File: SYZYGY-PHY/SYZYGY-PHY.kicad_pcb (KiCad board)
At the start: 4 copper layers, 57.7 x 28 mm, 37 parts, among them J1 QTH-020-01-X-D-DP-A, J2 ARJM11C7-502-KB-EW2, J3 Conn_01x08, U1 GPY111, Y1 Crystal_GND24

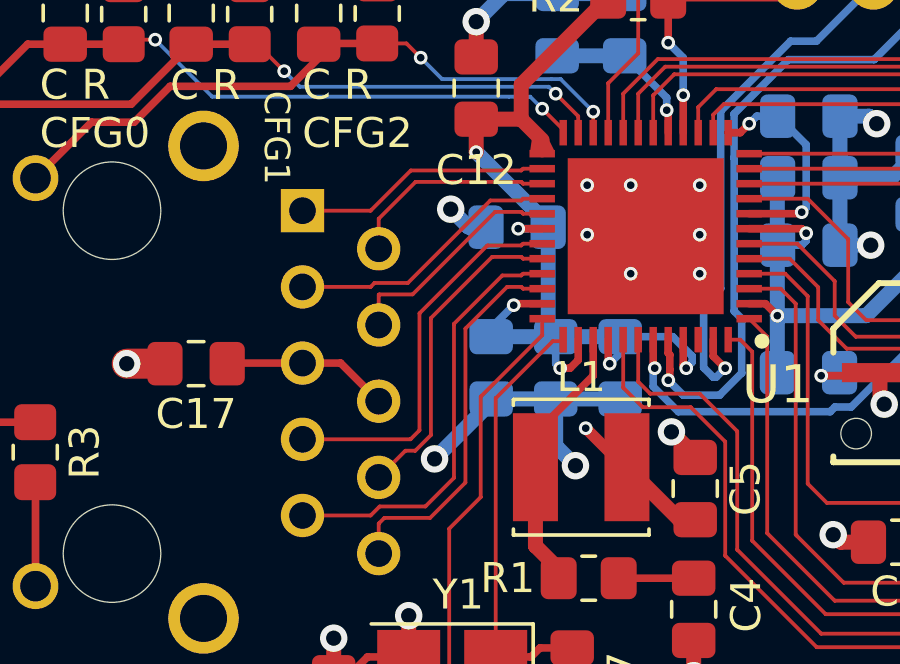
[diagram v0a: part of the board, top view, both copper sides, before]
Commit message: fixing diff pair skew from the twisted pair interface
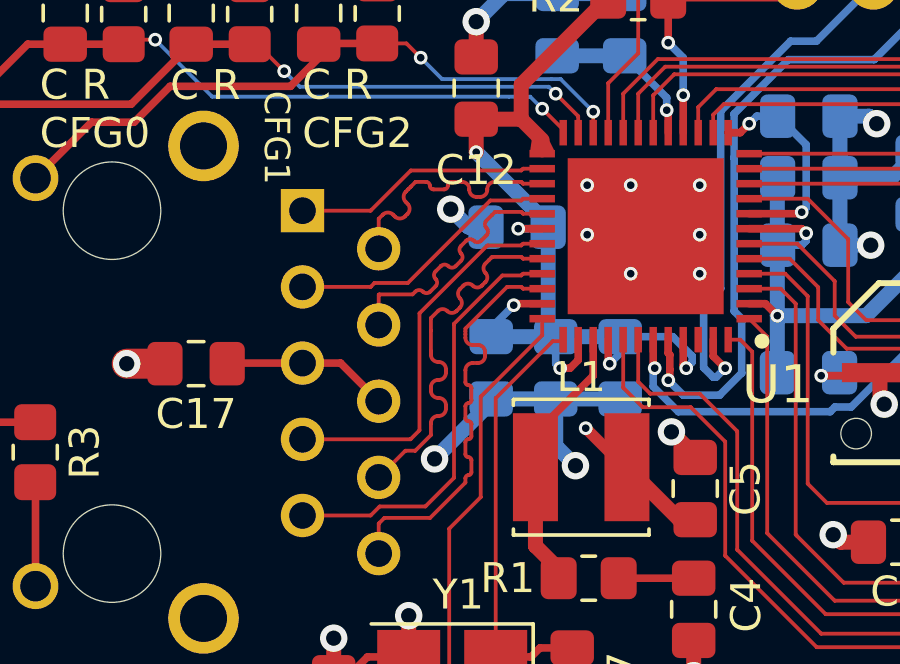
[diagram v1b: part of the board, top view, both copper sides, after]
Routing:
- net /TD3-: track 10.8 -> 12.8 mm
- net /TD4-: track 12.8 -> 14.2 mm
- net /TD1-: track 6.98 -> 8.47 mm
- net /TD2-: track 7.62 -> 8.74 mm

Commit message: syzygy todo update
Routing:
- net GND: vias 35 -> 82

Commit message: wibbly wobbly
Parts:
- removed C3: 10u, Capacitor_SMD:C_0805_2012Metric_Pad1.18x1.45mm_HandSolder
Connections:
- J1 pad 39: +1V8 -> unconnected-(J1-Pad39)
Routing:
- net /TXD3: track 9.62 -> 17.9 mm
- net /TXD2: track 10.4 -> 17.9 mm
- net /RX_CLK: track 18.6 -> 23.8 mm
- net /RXD0: track 19.4 -> 23.8 mm
- net /RXD1: track 19.9 -> 23.9 mm
- net +1V8: track 3.14 -> 0.00 mm, vias 2 -> 0
- net /TXD1: track 14.8 -> 17.8 mm
- net /RXD3: track 25.0 -> 23.9 mm
- net /RXD2: track 24.9 -> 23.8 mm
- net GND: track 80.2 -> 79.8 mm, vias 82 -> 34

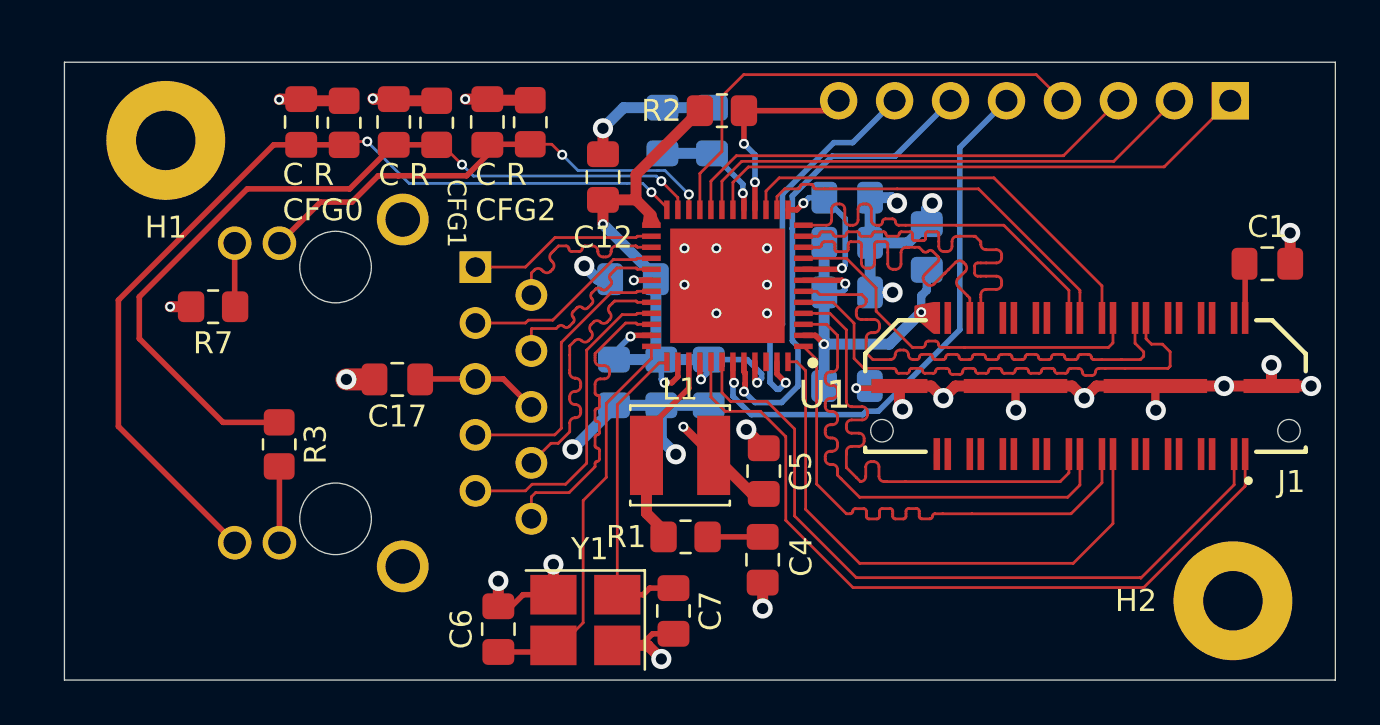
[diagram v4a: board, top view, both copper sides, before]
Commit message: picking a concrete inductor and updating footprint, breakout out MDC/MDIO into headers instead of SYZYGY, corrected rules and text labels
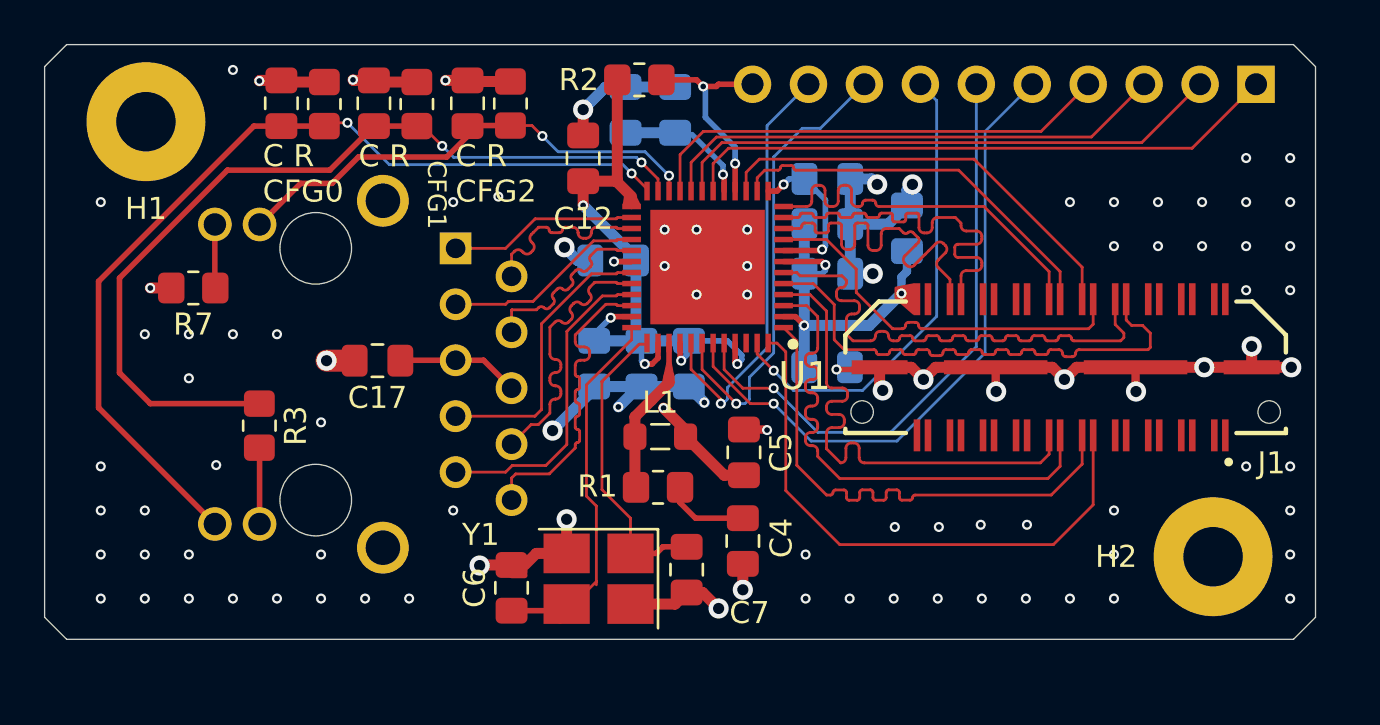
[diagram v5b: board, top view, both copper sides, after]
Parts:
- removed C1: 10u, Capacitor_SMD:C_0805_2012Metric_Pad1.18x1.45mm_HandSolder
- J3: value Conn_01x08 -> Conn_01x10; footprint Connector_PinSocket_2.54mm:PinSocket_1x08_P2.54mm_Vertical -> Connector_PinSocket_2.54mm:PinSocket_1x10_P2.54mm_Vertical
- L1: footprint Inductor_SMD:L_Abracon_ASPI-0425 -> Inductor_SMD:L_0805_2012Metric_Pad1.05x1.20mm_HandSolder
- moved R2 4.00 mm to (117.0, 63.6)
- moved R1 2.57 mm to (117.8, 82.1)
- moved H2 2.19 mm to (143.1, 85.2)
- moved C6 1.97 mm to (111.2, 86.7)
- moved C7 1.97 mm to (119.2, 85.8)
- moved Y1 1.97 mm to (115.2, 86.2)
- moved C16 1.92 mm to (116.4, 65.0)
- moved C18 1.92 mm to (118.6, 65.0)
- moved J3 1.39 mm to (145.0, 63.8)
- moved C13 1.24 mm to (115.8, 71.8)
- moved C15 1.24 mm to (117.1, 76.5)
- moved C17 1.24 mm to (105.1, 76.3)
- moved C19 1.24 mm to (125.5, 68.1)
- moved C20 1.24 mm to (100.8, 64.7)
- moved C8 1.24 mm to (119.2, 76.5)
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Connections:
- J1 pad 01: /MDC -> unconnected-(J1-Pad01)
- J1 pad 02: +5V -> unconnected-(J1-Pad02)
- J1 pad 03: /MDIO -> unconnected-(J1-Pad03)
- J3 pad 8: /RSTN -> /MDIO
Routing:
- net /MDC: track 35.0 -> 19.5 mm, vias 0 -> 1
- net /MDIO: track 33.6 -> 21.0 mm, vias 0 -> 1
- net /SDA: track 22.1 -> 27.4 mm
- net /SCL: track 25.1 -> 29.6 mm
- net /MDINT: track 17.7 -> 21.6 mm
- net GND: track 79.8 -> 77.3 mm, vias 34 -> 96
- net +5V: track 2.47 -> 0.00 mm
- net /REG0: track 9.07 -> 6.61 mm
- net /TCK: track 23.4 -> 25.4 mm
- net /TDI: track 25.4 -> 27.4 mm
- net /TMS: track 21.3 -> 23.3 mm
- net /XTAL1: track 18.2 -> 16.8 mm
- net /LED1: track 38.7 -> 40.1 mm
- net Net-(C4-Pad2): track 2.50 -> 3.84 mm
- net +3V3: track 57.6 -> 57.0 mm
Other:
- board size 57.7 x 28 mm -> 57.7 x 27 mm
- board text added: "MDC"
- board text added: "MDIO"

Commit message: adding another mounting hole for a more stable 3 mounts
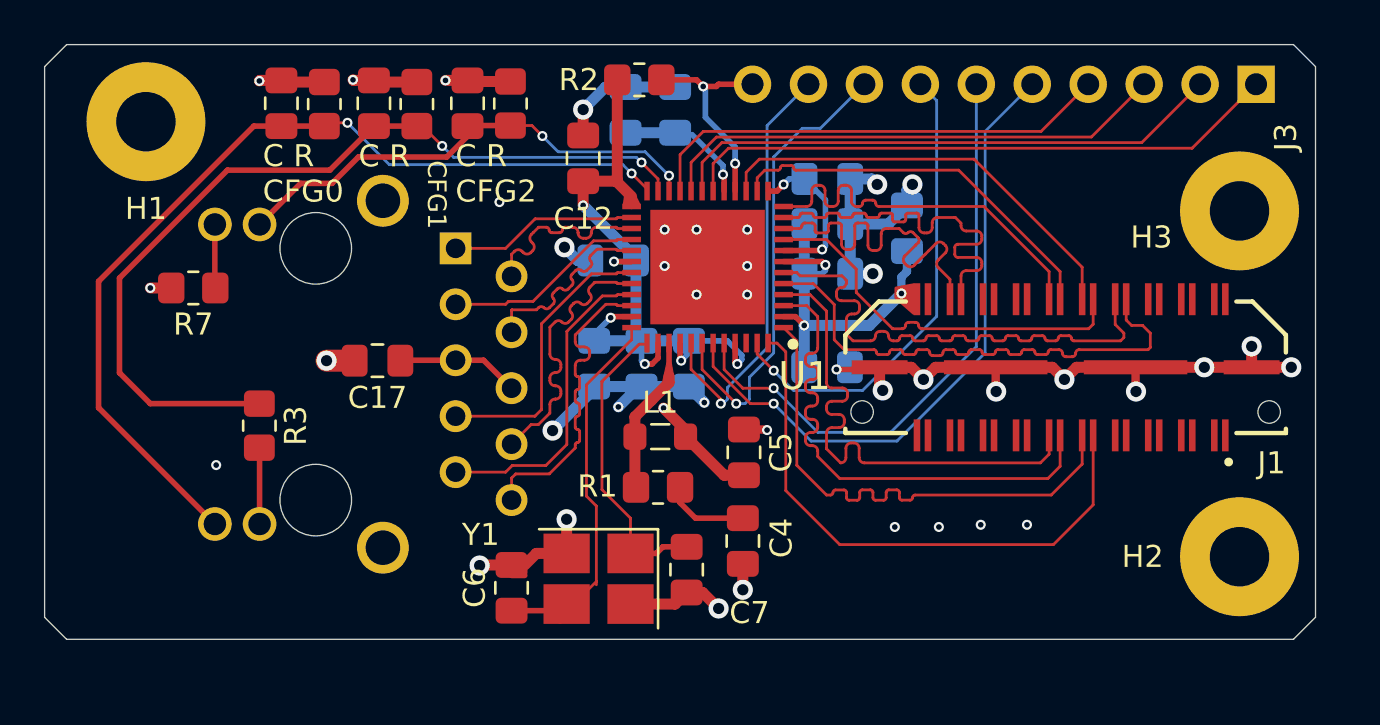
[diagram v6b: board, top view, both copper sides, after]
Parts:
- added H3: MountingHole_Pad, MountingHole:MountingHole_2.7mm_M2.5_Pad, F.Cu at (144.2, 69.5)
- moved H2 1.20 mm to (144.2, 85.2)
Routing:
- net GND: vias 96 -> 40

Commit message: adding GND stippling
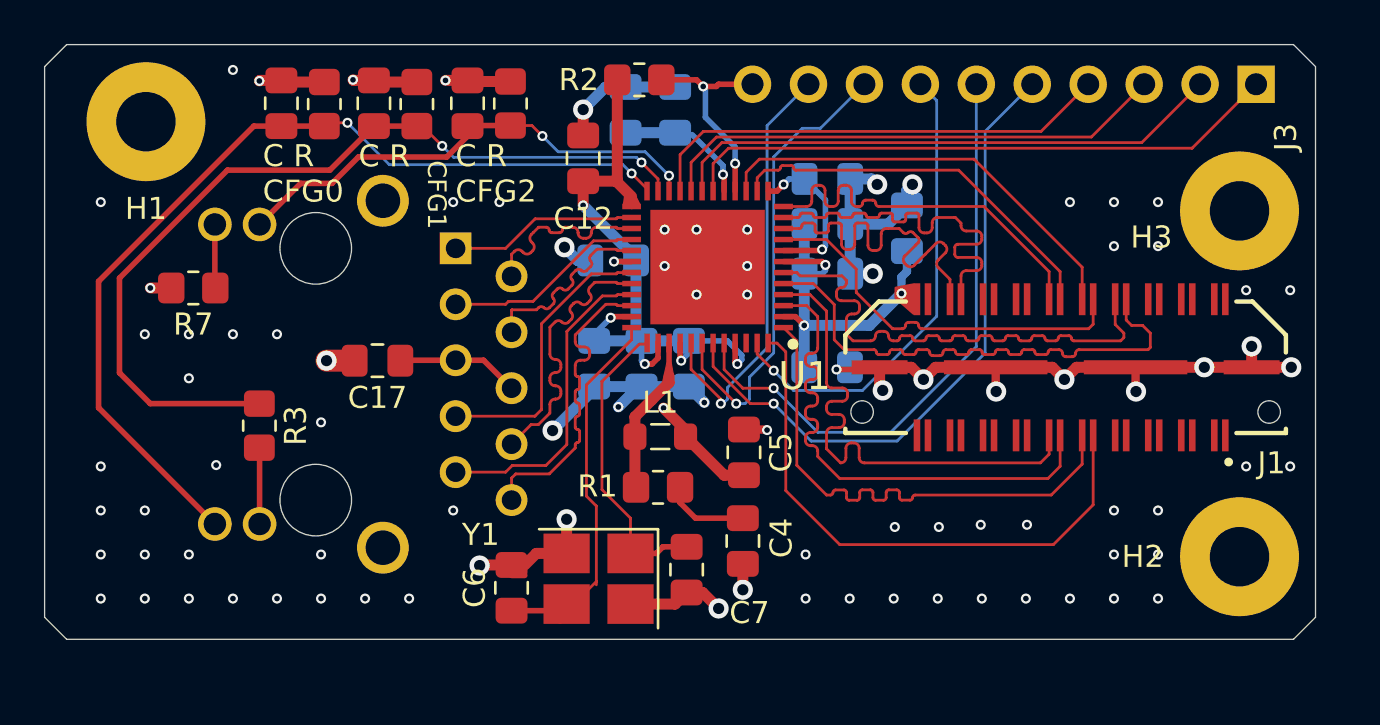
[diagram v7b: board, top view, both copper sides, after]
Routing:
- net GND: vias 40 -> 88

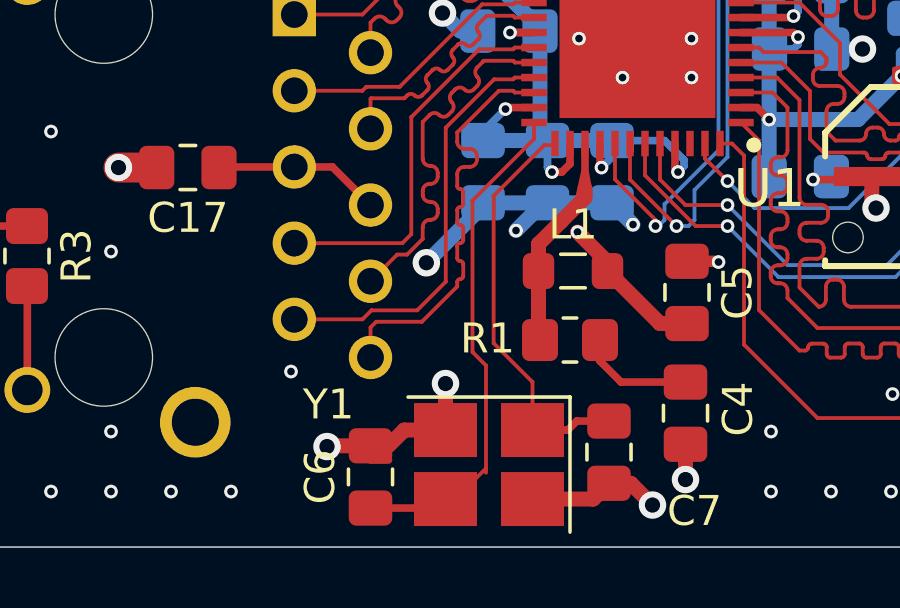
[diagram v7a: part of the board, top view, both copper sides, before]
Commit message: updating the caps and crystal, confirming the crystal circuit and footprints
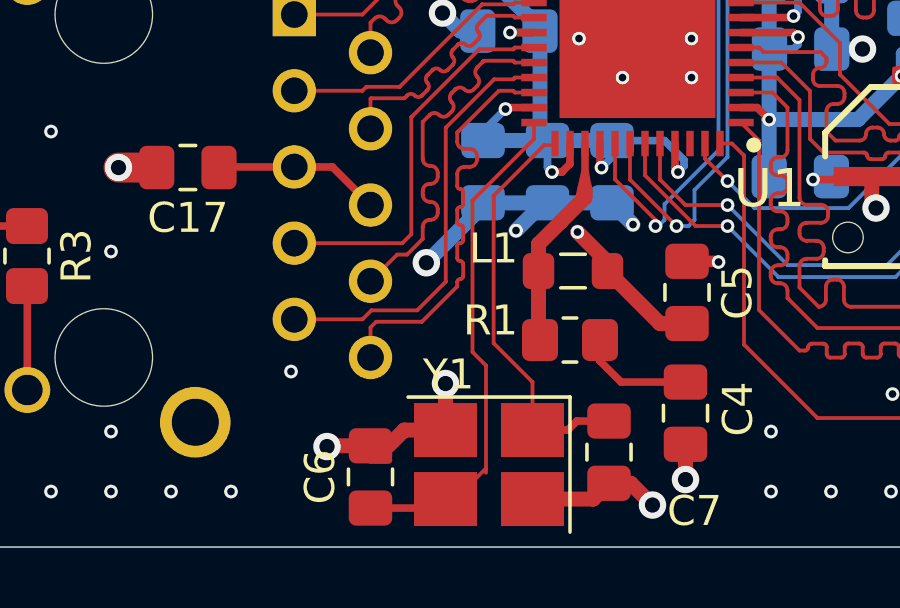
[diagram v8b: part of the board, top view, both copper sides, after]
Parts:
- C6, C7: value 18p -> 33p
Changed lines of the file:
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@@
 		(tags "inductor handsolder")
 		(property "Reference" "L1"
-			(at 0 -1.55 0)
+			(at -2.65 -0.75 0)
 			(layer "F.SilkS")
 			(effects
@@
 			)
 		)
-		(property "Value" "18p"
+		(property "Value" "33p"
 			(at 0 1.68 90)
 			(layer "F.Fab")
@@
 		(tags "SMD SMT crystal hand-soldering")
 		(property "Reference" "Y1"
-			(at 5.35 2 0)
+			(at 1.35 3 0)
 			(layer "F.SilkS")
 			(effects
@@
 			)
 		)
-		(property "Datasheet" ""
+		(property "Datasheet" "https://www.mouser.com/datasheet/2/137/FA_238_en-932914.pdf"
 			(at 0 0 180)
 			(unlocked yes)
@@
 			)
 		)
+		(property "Mouser" "FA-238 25.0000MB-I "
+			(at 0 0 180)
+			(unlocked yes)
+			(layer "F.Fab")
+			(hide yes)
+			(effects
+				(font
+					(size 1 1)
+					(thickness 0.15)
+				)
+			)
+		)
 		(property ki_fp_filters "Crystal*")
 		(sheetname "Root")
@@
 		(tags "resistor handsolder")
 		(property "Reference" "R1"
-			(at -2.75 -0.05 0)
+			(at -2.65 -0.65 0)
 			(layer "F.SilkS")
 			(effects
@@
 			)
 		)
-		(property "Value" "18p"
+		(property "Value" "33p"
 			(at 0 1.68 90)
 			(layer "F.Fab")
